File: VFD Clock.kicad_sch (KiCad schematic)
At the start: 33 parts, among them J1 DS3231, J2 Mode Button, J3 Up Button, J4 Down Button, J5 Select Button, U1 74HC595, U10 74HC595, U11 UDN2981A, U12 Minute Right, U13 74HC595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

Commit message: minor changes
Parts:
- J2, J3, J4, J5: footprint (none) -> Connector_JST:JST_XH_B2B-XH-A_1x02_P2.50mm_Vertical
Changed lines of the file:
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@@
 			)
 		)
-		(property "Footprint" ""
+		(property "Footprint" "Connector_JST:JST_XH_B2B-XH-A_1x02_P2.50mm_Vertical"
 			(at 220.98 299.72 0)
 			(hide yes)
@@
 			)
 		)
-		(property "Footprint" ""
+		(property "Footprint" "Connector_JST:JST_XH_B2B-XH-A_1x02_P2.50mm_Vertical"
 			(at 222.25 323.85 0)
 			(hide yes)
@@
 			)
 		)
-		(property "Footprint" ""
+		(property "Footprint" "Connector_JST:JST_XH_B2B-XH-A_1x02_P2.50mm_Vertical"
 			(at 220.98 312.42 0)
 			(hide yes)
@@
 			)
 		)
-		(property "Footprint" ""
+		(property "Footprint" "Connector_JST:JST_XH_B2B-XH-A_1x02_P2.50mm_Vertical"
 			(at 219.71 288.29 0)
 			(hide yes)

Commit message: Created custom ds3231 module and added it to schematic and pcb
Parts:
- removed J1: DS3231, symbol Connector:Conn_01x04_Socket
- added U21: DS3231 Module, Custom Parts:DS3231 Module, symbol Custom Parts:DS3231_Module
- J2, J3, J4, J5: footprint Connector_JST:JST_XH_B2B-XH-A_1x02_P2.50mm_Vertical -> Connector_PinHeader_2.54mm:PinHeader_1x02_P2.54mm_Vertical
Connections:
- net +5V: now also U21.2 (VCC)
- net GND: now also U21.1 (GND)
- net SCL: now also U21.4 (SCL)
- net SDA: now also U21.3 (SDA)
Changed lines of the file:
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@@
 	(wire
 		(pts
-			(xy 180.34 302.26) (xy 185.42 302.26)
+			(xy 168.91 298.45) (xy 163.83 298.45)
 		)
 		(stroke
@@
 	(wire
 		(pts
-			(xy 180.34 304.8) (xy 185.42 304.8)
+			(xy 168.91 295.91) (xy 163.83 295.91)
 		)
 		(stroke
@@
 	)
 	(label "SCL"
-		(at 185.42 304.8 0)
+		(at 163.83 295.91 180)
 		(effects
 			(font
 				(size 1.27 1.27)
 			)
-			(justify left bottom)
+			(justify right bottom)
 		)
 	)
@@
 	)
 	(label "SDA"
-		(at 185.42 302.26 0)
+		(at 163.83 298.45 180)
 		(effects
 			(font
 				(size 1.27 1.27)
 			)
-			(justify left bottom)
+			(justify right bottom)
 		)
 	)
@@
 			)
 		)
-		(property "Footprint" "Connector_JST:JST_XH_B2B-XH-A_1x02_P2.50mm_Vertical"
+		(property "Footprint" "Connector_PinHeader_2.54mm:PinHeader_1x02_P2.54mm_Vertical"
 			(at 220.98 299.72 0)
 			(hide yes)
@@
 	)
 	(symbol
+		(lib_id "Custom Parts:DS3231_Module")
+		(at 168.91 293.37 0)
+		(unit 1)
+		(body_style 1)
+		(exclude_from_sim no)
+		(in_bom yes)
+		(on_board yes)
+		(in_pos_files yes)
+		(dnp no)
+		(fields_autoplaced yes)
+		(property "Reference" "U21"
+			(at 177.8 297.8149 0)
+			(show_name no)
+			(do_not_autoplace no)
+			(effects
+				(font
+					(size 1.27 1.27)
+				)
+				(justify left)
+			)
+		)
+		(property "Value" "DS3231 Module"
+			(at 177.8 300.3549 0)
+			(show_name no)
+			(do_not_autoplace no)
+			(effects
+				(font
+					(size 1.27 1.27)
+				)
+				(justify left)
+			)
+		)
+		(property "Footprint" "Custom Parts:DS3231 Module"
+			(at 168.91 293.37 0)
+			(hide yes)
+			(show_name no)
+			(do_not_autoplace no)
+			(effects
+				(font
+					(size 1.27 1.27)
+				)
+			)
+		)
+		(property "Datasheet" ""
+			(at 168.91 293.37 0)
+			(hide yes)
+			(show_name no)
+			(do_not_autoplace no)
+			(effects
+				(font
+					(size 1.27 1.27)
+				)
+			)
+		)
+		(property "Description" ""
+			(at 168.91 293.37 0)
+			(hide yes)
+			(show_name no)
+			(do_not_autoplace no)
+			(effects
+				(font
+					(size 1.27 1.27)
+				)
+			)
+		)
+		(pin "4"
+		)
+		(pin "1"
+		)
+		(pin "2"
+		)
+		(pin "3"
+		)
+		(instances
+			(project "VFD Clock"
+				(path "/18b1ce2b-a4eb-4908-8bcd-bbd2350e3040"
+					(reference "U21")
+					(unit 1)
+				)
+			)
+		)
+	)
+	(symbol
 		(lib_id "74xx:74HC595")
 		(at 49.53 95.25 0)
@@
 			)
 		)
-		(property "Footprint" "Connector_JST:JST_XH_B2B-XH-A_1x02_P2.50mm_Vertical"
+		(property "Footprint" "Connector_PinHeader_2.54mm:PinHeader_1x02_P2.54mm_Vertical"
 			(at 222.25 323.85 0)
 			(hide yes)
@@
 			)
 		)
-		(property "Footprint" "Connector_JST:JST_XH_B2B-XH-A_1x02_P2.50mm_Vertical"
+		(property "Footprint" "Connector_PinHeader_2.54mm:PinHeader_1x02_P2.54mm_Vertical"
 			(at 220.98 312.42 0)
 			(hide yes)
@@
 	(symbol
 		(lib_id "power:+5V")
-		(at 180.34 299.72 270)
+		(at 168.91 300.99 90)
 		(unit 1)
 		(body_style 1)
@@
 		(in_pos_files yes)
 		(dnp no)
-		(fields_autoplaced yes)
 		(property "Reference" "#PWR072"
-			(at 176.53 299.72 0)
+			(at 172.72 300.99 0)
 			(hide yes)
 			(show_name no)
@@
 		)
 		(property "Value" "+5V"
-			(at 184.15 299.7199 90)
+			(at 163.83 301.244 90)
 			(show_name no)
 			(do_not_autoplace no)
@@
 					(size 1.27 1.27)
 				)
-				(justify left)
 			)
 		)
 		(property "Footprint" ""
-			(at 180.34 299.72 0)
+			(at 168.91 300.99 0)
 			(hide yes)
 			(show_name no)
@@
 		)
 		(property "Datasheet" ""
-			(at 180.34 299.72 0)
+			(at 168.91 300.99 0)
 			(hide yes)
 			(show_name no)
@@
 		)
 		(property "Description" "Power symbol creates a global label with name \"+5V\""
-			(at 180.34 299.72 0)
+			(at 168.91 300.99 0)
 			(hide yes)
 			(show_name no)
@@
 			)
 		)
-		(property "Footprint" "Connector_JST:JST_XH_B2B-XH-A_1x02_P2.50mm_Vertical"
+		(property "Footprint" "Connector_PinHeader_2.54mm:PinHeader_1x02_P2.54mm_Vertical"
 			(at 219.71 288.29 0)
 			(hide yes)
@@
 	(symbol
 		(lib_id "power:GND")
-		(at 180.34 297.18 90)
+		(at 168.91 303.53 270)
 		(unit 1)
 		(body_style 1)
@@
 		(in_pos_files yes)
 		(dnp no)
-		(fields_autoplaced yes)
 		(property "Reference" "#PWR071"
-			(at 186.69 297.18 0)
+			(at 162.56 303.53 0)
 			(hide yes)
 			(show_name no)
@@
 		)
 		(property "Value" "GND"
-			(at 184.15 297.1799 90)
+			(at 163.576 303.53 90)
 			(show_name no)
 			(do_not_autoplace no)
@@
 					(size 1.27 1.27)
 				)
-				(justify right)
 			)
 		)
 		(property "Footprint" ""
-			(at 180.34 297.18 0)
+			(at 168.91 303.53 0)
 			(hide yes)
 			(show_name no)
@@
 		)
 		(property "Datasheet" ""
-			(at 180.34 297.18 0)
+			(at 168.91 303.53 0)
 			(hide yes)
 			(show_name no)
@@
 		)
 		(property "Description" "Power symbol creates a global label with name \"GND\" , ground"
-			(at 180.34 297.18 0)
+			(at 168.91 303.53 0)
 			(hide yes)
 			(show_name no)
@@
 					(unit 1)
 				)
-			)
-		)
-	)
-	(symbol
-		(lib_id "Connector:Conn_01x04_Socket")
-		(at 175.26 302.26 180)
-		(unit 1)
-		(body_style 1)
-		(exclude_from_sim no)
-		(in_bom yes)
-		(on_board yes)
-		(in_pos_files yes)
-		(dnp no)
-		(fields_autoplaced yes)
-		(property "Reference" "J1"
-			(at 175.895 292.1 0)
-			(show_name no)
-			(do_not_autoplace no)
-			(effects
-				(font
-					(size 1.27 1.27)
-				)
-			)
-		)
-		(property "Value" "DS3231"
-			(at 175.895 294.64 0)
-			(show_name no)
-			(do_not_autoplace no)
-			(effects
-				(font
-					(size 1.27 1.27)
-				)
-			)
-		)
-		(property "Footprint" ""
-			(at 175.26 302.26 0)
-			(hide yes)
-			(show_name no)
-			(do_not_autoplace no)
-			(effects
-				(font
-					(size 1.27 1.27)
-				)
-			)
-		)
-		(property "Datasheet" ""
-			(at 175.26 302.26 0)
-			(hide yes)
-			(show_name no)
-			(do_not_autoplace no)
-			(effects
-				(font
-					(size 1.27 1.27)
-				)
-			)
-		)
-		(property "Description" "Generic connector, single row, 01x04, script generated"
-			(at 175.26 302.26 0)
-			(hide yes)
-			(show_name no)
-			(do_not_autoplace no)
-			(effects
-				(font
-					(size 1.27 1.27)
-				)
-			)
-		)
-		(pin "3"
-		)
-		(pin "1"
-		)
-		(pin "4"
-		)
-		(pin "2"
-		)
-		(instances
-			(project "VFD Clock"
-				(path "/18b1ce2b-a4eb-4908-8bcd-bbd2350e3040"
-					(reference "J1")
-					(unit 1)
-				)

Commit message: save
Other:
- moved on the sheet: A1, C1, J2, J3, J4, J5, U19, U20, U21

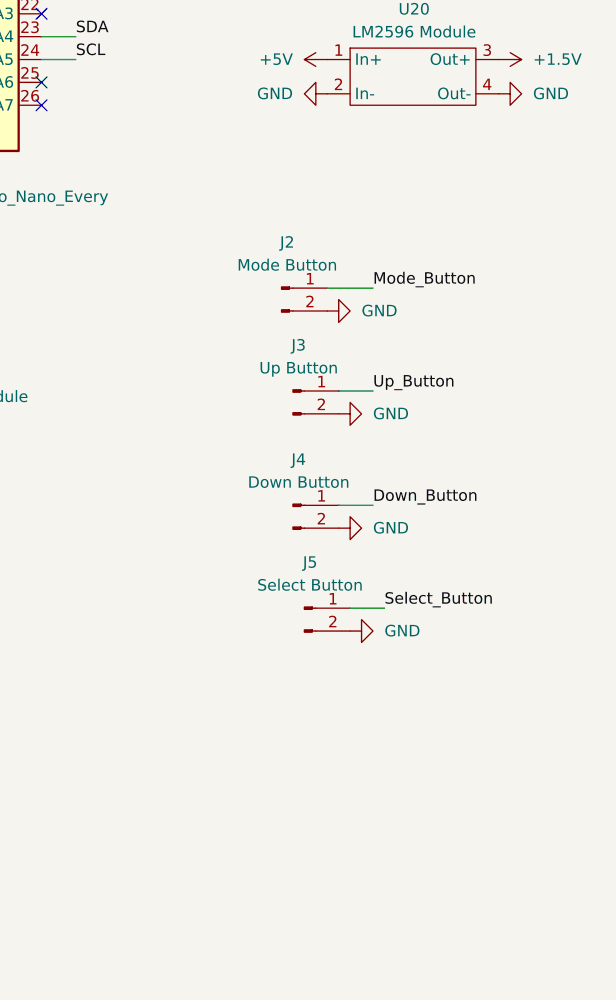
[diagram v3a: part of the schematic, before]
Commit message: add debouncing caps
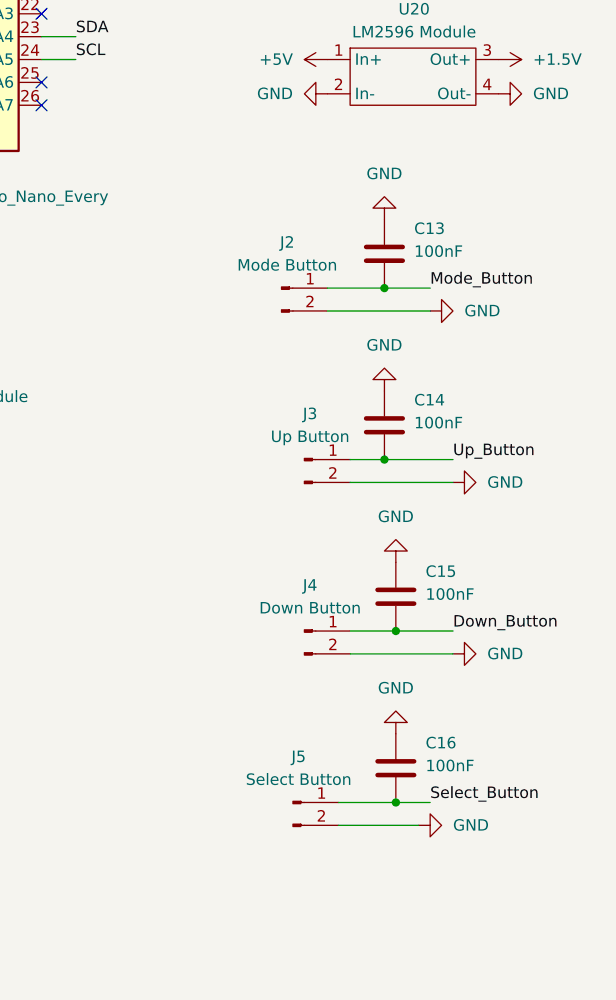
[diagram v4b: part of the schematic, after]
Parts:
- added C13, C14, C15, C16: 100nF, Capacitor_THT:C_Disc_D3.0mm_W1.6mm_P2.50mm, symbol Device:C
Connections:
- net Down_Button: now also C15.2
- net GND: now also C13.1, C14.1, C15.1, C16.1
- net Mode_Button: now also C13.2
- net Select_Button: now also C16.2
- net Up_Button: now also C14.2
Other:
- moved on the sheet: J3, J4, J5

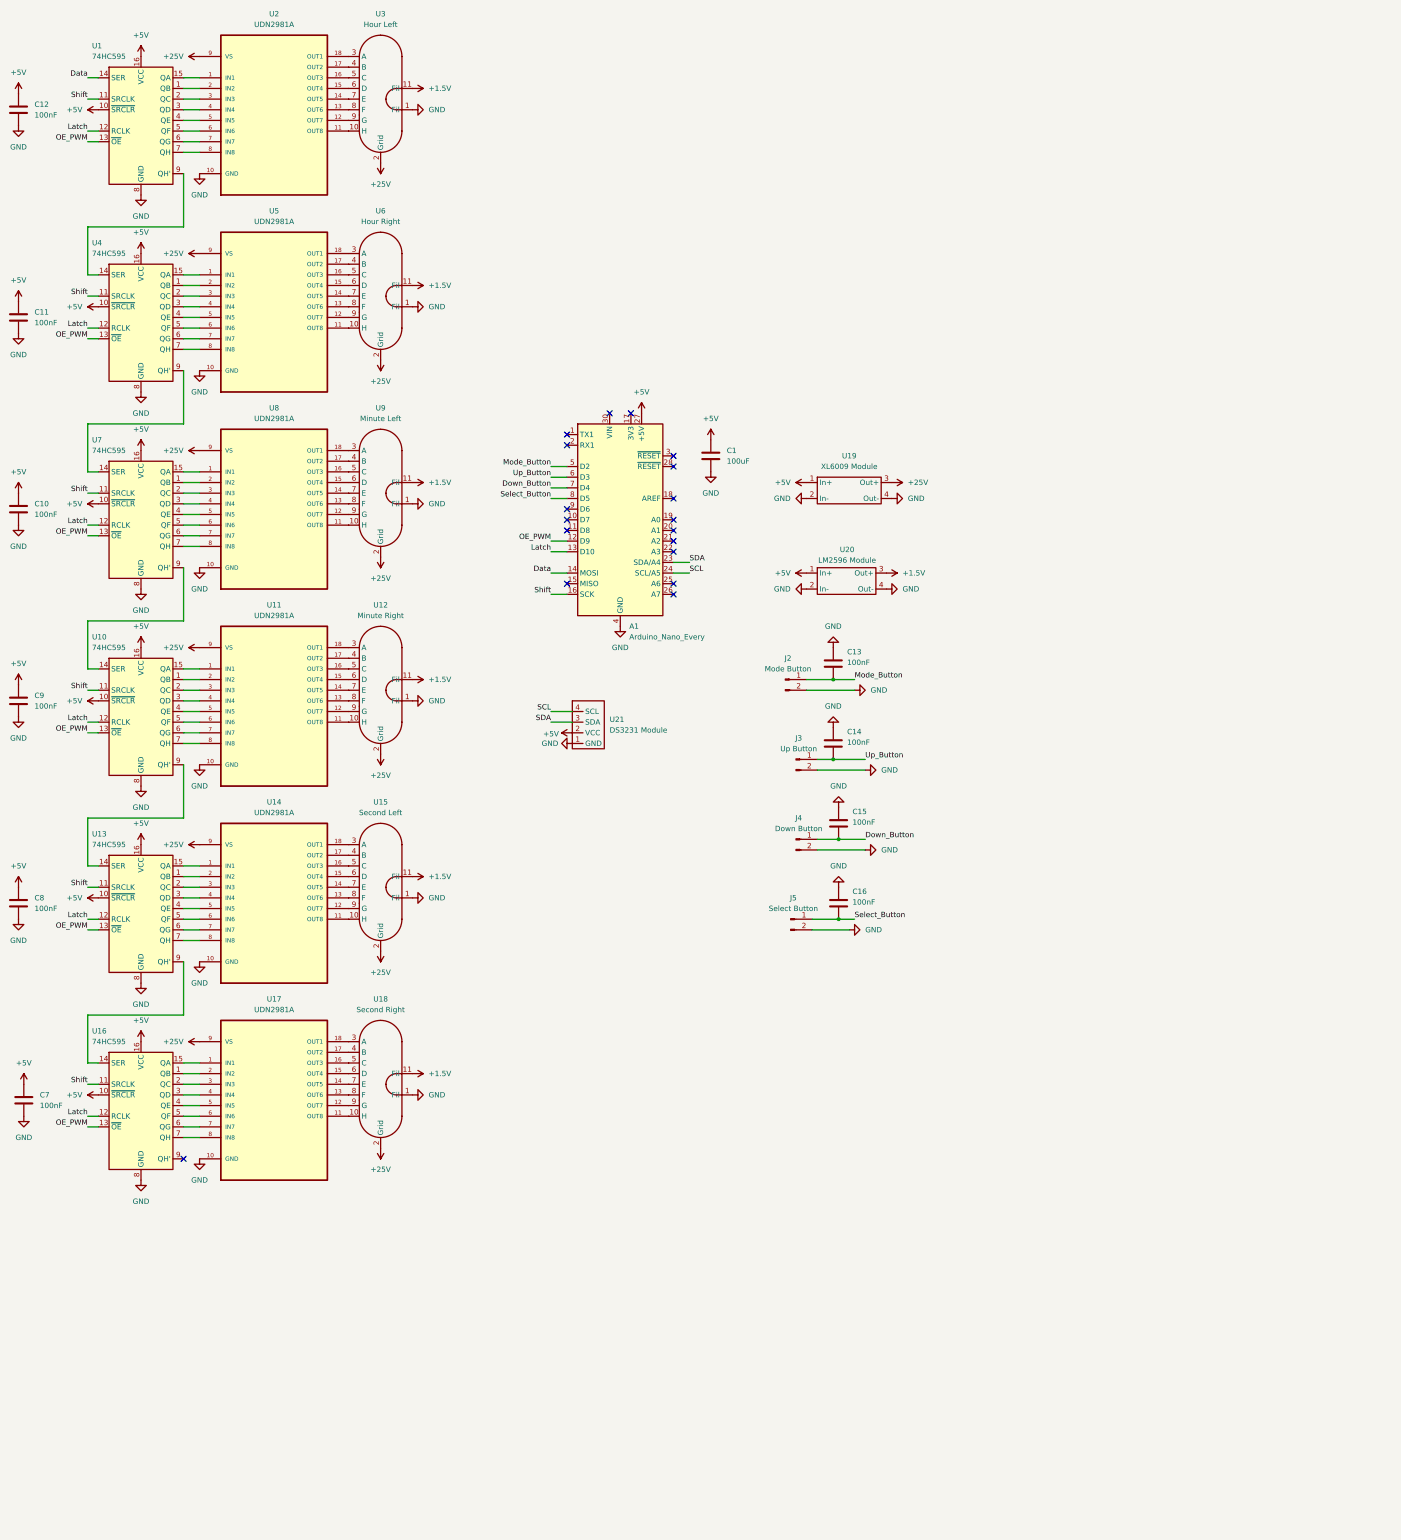
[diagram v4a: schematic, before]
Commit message: schematic ordering
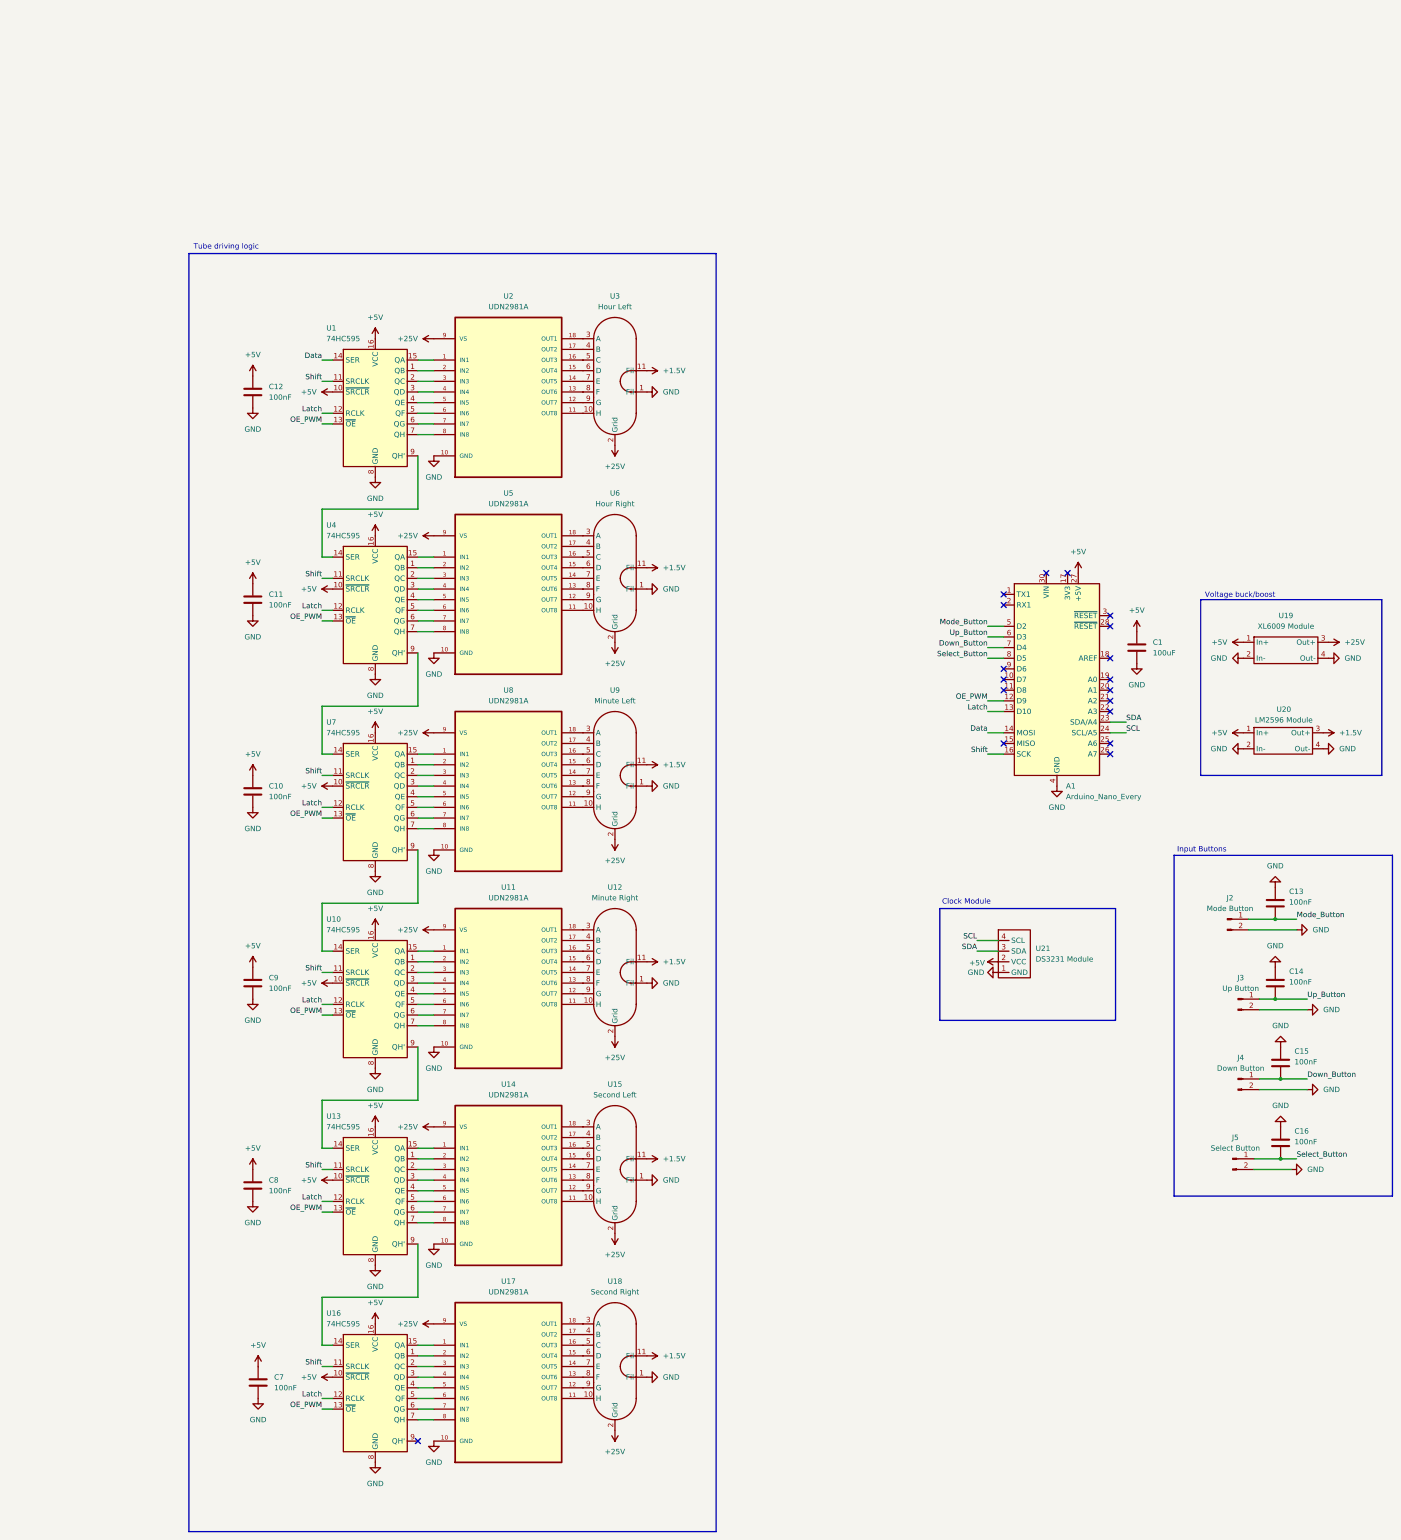
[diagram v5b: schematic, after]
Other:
- note added: "Clock Module"
- note added: "Input Buttons"
- note added: "Tube driving logic"
- note added: "Voltage buck/boost"
- moved on the sheet: A1, C1, C10, C11, C12, C13, C14, C15, C16, C7, C8, C9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

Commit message: checkpoint
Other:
- note added: "Arduino Nano control"
- moved on the sheet: A1, C1
